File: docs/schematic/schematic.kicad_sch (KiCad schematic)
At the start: 24 parts, among them J101 Analog Levers, J12 Button Matrix, J13 Front LED, J5 Motor-PCB, J6 X-Axis, J7 Y-Axis, J8 Z-Axis, Q1 BC548, U1 ProMicroC, U101 74HC4066BQ

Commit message: update wiring
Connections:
- net GND: now also U1.11 (D8/A8); no longer U1.13 (D10/A10)
- net Matrix_Row3: now also U1.1 (TX); no longer U1.11 (D8/A8)
- no-connect marks 14 -> 13
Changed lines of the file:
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@@
-	)
-	(no_connect
-		(at 109.22 53.34)
 	)
 	(no_connect
@@
 	(wire
 		(pts
-			(xy 135.89 53.34) (xy 133.35 53.34)
-		)
-		(stroke
-			(width 0)
-			(type default)
-		)
-	)
-	(wire
-		(pts
 			(xy 170.18 29.21) (xy 167.64 29.21)
 		)
@@
 	(wire
 		(pts
-			(xy 133.35 48.26) (xy 139.7 48.26)
-		)
-		(stroke
-			(width 0)
-			(type default)
-		)
-	)
-	(wire
-		(pts
 			(xy 55.88 49.53) (xy 55.88 55.88)
 		)
@@
 	(wire
 		(pts
-			(xy 133.35 45.72) (xy 139.7 45.72)
+			(xy 133.35 45.72) (xy 137.16 45.72)
 		)
 		(stroke
@@
 	(wire
 		(pts
-			(xy 133.35 71.12) (xy 135.89 71.12)
-		)
-		(stroke
-			(width 0)
-			(type default)
-		)
-	)
-	(wire
-		(pts
-			(xy 133.35 60.96) (xy 138.43 60.96)
+			(xy 133.35 71.12) (xy 137.16 71.12)
+		)
+		(stroke
+			(width 0)
+			(type default)
+		)
+	)
+	(wire
+		(pts
+			(xy 133.35 60.96) (xy 137.16 60.96)
 		)
 		(stroke
@@
 	(wire
 		(pts
+			(xy 133.35 48.26) (xy 137.16 48.26)
+		)
+		(stroke
+			(width 0)
+			(type default)
+		)
+	)
+	(wire
+		(pts
 			(xy 166.37 93.98) (xy 198.12 93.98)
 		)
@@
 	(wire
 		(pts
-			(xy 133.35 58.42) (xy 138.43 58.42)
+			(xy 133.35 58.42) (xy 137.16 58.42)
 		)
 		(stroke
@@
 		(pts
 			(xy 245.11 138.43) (xy 245.11 139.7)
+		)
+		(stroke
+			(width 0)
+			(type default)
+		)
+	)
+	(wire
+		(pts
+			(xy 105.41 53.34) (xy 109.22 53.34)
 		)
 		(stroke
@@
 	(global_label "Matrix_Col3"
 		(shape input)
-		(at 138.43 60.96 0)
+		(at 137.16 60.96 0)
 		(fields_autoplaced yes)
 		(effects
@@
 		)
 		(property "Intersheetrefs" "${INTERSHEET_REFS}"
-			(at 152.4217 60.96 0)
+			(at 151.1517 60.96 0)
 			(effects
 				(font
@@
 		)
 	)
-	(global_label "A10"
+	(global_label "A8"
 		(shape output)
 		(at 121.92 165.1 0)
@@
 		)
 		(property "Intersheetrefs" "${INTERSHEET_REFS}"
-			(at 128.4128 165.1 0)
+			(at 127.2033 165.1 0)
 			(effects
 				(font
@@
 	(global_label "Matrix_Row2"
 		(shape output)
-		(at 139.7 45.72 0)
+		(at 137.16 45.72 0)
 		(fields_autoplaced yes)
 		(effects
@@
 		)
 		(property "Intersheetrefs" "${INTERSHEET_REFS}"
-			(at 154.357 45.72 0)
+			(at 151.817 45.72 0)
 			(effects
 				(font
@@
 		)
 	)
-	(global_label "A10"
+	(global_label "A8"
 		(shape output)
 		(at 80.01 165.1 0)
@@
 		)
 		(property "Intersheetrefs" "${INTERSHEET_REFS}"
-			(at 86.5028 165.1 0)
+			(at 85.2933 165.1 0)
 			(effects
 				(font
@@
 	(global_label "Matrix_Col2"
 		(shape input)
-		(at 138.43 58.42 0)
+		(at 137.16 58.42 0)
 		(fields_autoplaced yes)
 		(effects
@@
 		)
 		(property "Intersheetrefs" "${INTERSHEET_REFS}"
-			(at 152.4217 58.42 0)
+			(at 151.1517 58.42 0)
 			(effects
 				(font
@@
 	(global_label "A3"
 		(shape input)
-		(at 135.89 71.12 0)
+		(at 137.16 71.12 0)
 		(fields_autoplaced yes)
 		(effects
@@
 		)
 		(property "Intersheetrefs" "${INTERSHEET_REFS}"
-			(at 141.1733 71.12 0)
+			(at 142.4433 71.12 0)
 			(effects
 				(font
@@
 		)
 	)
-	(global_label "A10"
+	(global_label "A8"
 		(shape input)
-		(at 135.89 53.34 0)
+		(at 137.16 48.26 0)
 		(fields_autoplaced yes)
 		(effects
@@
 		)
 		(property "Intersheetrefs" "${INTERSHEET_REFS}"
-			(at 142.3828 53.34 0)
+			(at 142.4433 48.26 0)
 			(effects
 				(font
@@
 	(global_label "Matrix_Row3"
 		(shape output)
-		(at 139.7 48.26 0)
-		(fields_autoplaced yes)
-		(effects
-			(font
-				(size 1.27 1.27)
-			)
-			(justify left)
-		)
-		(property "Intersheetrefs" "${INTERSHEET_REFS}"
-			(at 154.357 48.26 0)
-			(effects
-				(font
-					(size 1.27 1.27)
-				)
-				(justify left)
-				(hide yes)
-			)
+		(at 105.41 53.34 180)
+		(fields_autoplaced yes)
+		(effects
+			(font
+				(size 1.27 1.27)
+			)
+			(justify right)
+		)
+		(property "Intersheetrefs" "${INTERSHEET_REFS}"
+			(at 90.753 53.34 0)
+			(effects
+				(font
+					(size 1.27 1.27)
+				)
+				(justify right)
+				(hide yes)
+			)

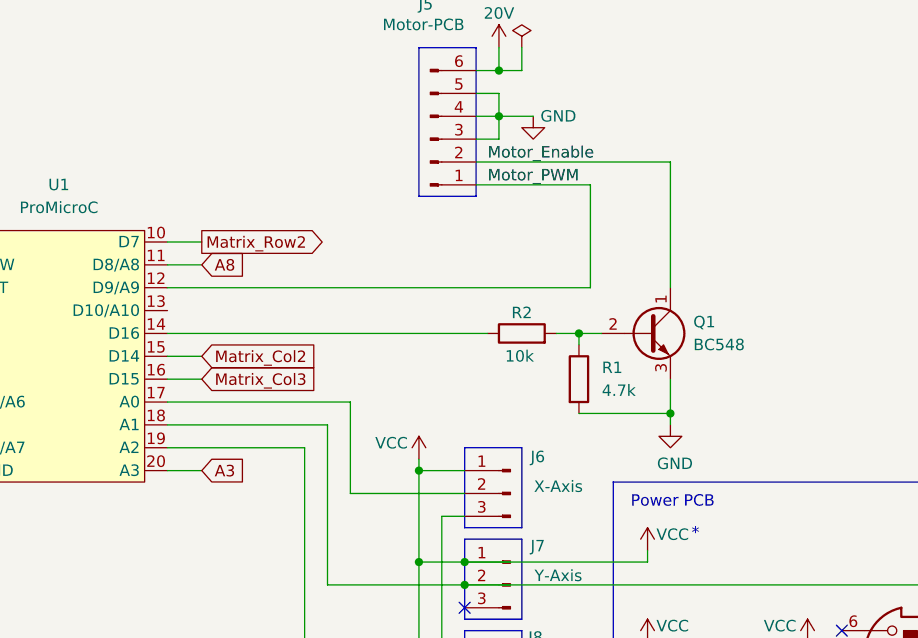
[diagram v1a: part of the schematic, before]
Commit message: update schematic
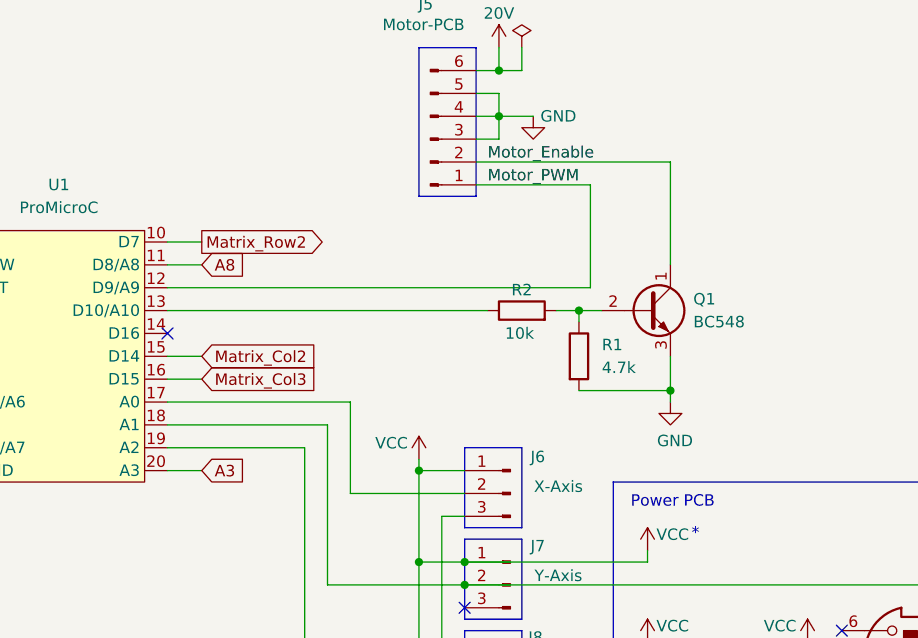
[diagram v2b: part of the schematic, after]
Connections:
- net at R2.1: now also U1.13 (D10/A10); no longer U1.14 (D16)
- no-connect marks 13 -> 14
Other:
- moved on the sheet: Q1, R1, R2
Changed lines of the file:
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@@
 	)
 	(junction
-		(at 189.23 64.77)
+		(at 189.23 62.23)
 		(diameter 0)
 		(color 0 0 0 0)
@@
 	)
 	(junction
-		(at 179.07 55.88)
-		(diameter 0)
-		(color 0 0 0 0)
-	)
-	(junction
 		(at 166.37 91.44)
 		(diameter 0)
@@
 	)
 	(junction
+		(at 179.07 53.34)
+		(diameter 0)
+		(color 0 0 0 0)
+	)
+	(junction
 		(at 170.18 31.75)
 		(diameter 0)
@@
 	)
 	(no_connect
+		(at 133.35 55.88)
+	)
+	(no_connect
 		(at 109.22 48.26)
 	)
@@
 	(wire
 		(pts
-			(xy 189.23 60.96) (xy 189.23 64.77)
-		)
-		(stroke
-			(width 0)
-			(type default)
-		)
-	)
-	(wire
-		(pts
 			(xy 59.69 63.5) (xy 69.85 63.5)
 		)
@@
 	(wire
 		(pts
-			(xy 189.23 36.83) (xy 189.23 50.8)
+			(xy 189.23 36.83) (xy 189.23 48.26)
 		)
 		(stroke
@@
 	(wire
 		(pts
-			(xy 133.35 55.88) (xy 168.91 55.88)
-		)
-		(stroke
-			(width 0)
-			(type default)
-		)
-	)
-	(wire
-		(pts
 			(xy 43.18 39.37) (xy 44.45 39.37)
 		)
@@
 	(wire
 		(pts
-			(xy 176.53 55.88) (xy 179.07 55.88)
+			(xy 176.53 53.34) (xy 179.07 53.34)
 		)
 		(stroke
@@
 	(wire
 		(pts
+			(xy 179.07 53.34) (xy 179.07 54.61)
+		)
+		(stroke
+			(width 0)
+			(type default)
+		)
+	)
+	(wire
+		(pts
 			(xy 170.18 31.75) (xy 170.18 29.21)
 		)
@@
 	(wire
 		(pts
-			(xy 179.07 55.88) (xy 181.61 55.88)
+			(xy 179.07 53.34) (xy 181.61 53.34)
 		)
 		(stroke
@@
 	(wire
 		(pts
+			(xy 189.23 58.42) (xy 189.23 62.23)
+		)
+		(stroke
+			(width 0)
+			(type default)
+		)
+	)
+	(wire
+		(pts
 			(xy 71.12 107.95) (xy 73.66 107.95)
 		)
@@
 	(wire
 		(pts
-			(xy 179.07 64.77) (xy 189.23 64.77)
+			(xy 179.07 62.23) (xy 189.23 62.23)
 		)
 		(stroke
@@
 	(wire
 		(pts
-			(xy 179.07 55.88) (xy 179.07 57.15)
-		)
-		(stroke
-			(width 0)
-			(type default)
-		)
-	)
-	(wire
-		(pts
 			(xy 133.35 48.26) (xy 137.16 48.26)
 		)
@@
 	(wire
 		(pts
-			(xy 189.23 66.04) (xy 189.23 64.77)
+			(xy 189.23 63.5) (xy 189.23 62.23)
 		)
 		(stroke
@@
 		)
 	)
+	(wire
+		(pts
+			(xy 133.35 53.34) (xy 168.91 53.34)
+		)
+		(stroke
+			(width 0)
+			(type default)
+		)
+	)
 	(label "Motor_Enable"
 		(at 168.91 36.83 0)
@@
 	(symbol
 		(lib_id "Device:R")
-		(at 172.72 55.88 90)
+		(at 172.72 53.34 90)
 		(unit 1)
 		(exclude_from_sim no)
@@
 		(dnp no)
 		(property "Reference" "R2"
-			(at 172.72 53.594 90)
+			(at 172.72 51.054 90)
 			(effects
 				(font
@@
 		)
 		(property "Value" "10k"
-			(at 172.466 58.42 90)
+			(at 172.466 55.88 90)
 			(effects
 				(font
@@
 		)
 		(property "Footprint" "Resistor_THT:R_Axial_DIN0207_L6.3mm_D2.5mm_P7.62mm_Horizontal"
-			(at 172.72 57.658 90)
+			(at 172.72 55.118 90)
 			(effects
 				(font
@@
 		)
 		(property "Datasheet" "~"
-			(at 172.72 55.88 0)
+			(at 172.72 53.34 0)
 			(effects
 				(font
@@
 		)
 		(property "Description" "Resistor"
-			(at 172.72 55.88 0)
+			(at 172.72 53.34 0)
 			(effects
 				(font
@@
 	(symbol
 		(lib_id "PCM_SparkFun-PowerSymbol:GND")
-		(at 189.23 66.04 0)
+		(at 189.23 63.5 0)
 		(unit 1)
 		(exclude_from_sim no)
@@
 		(dnp no)
 		(property "Reference" "#PWR013"
-			(at 189.23 72.39 0)
+			(at 189.23 69.85 0)
 			(effects
 				(font
@@
 		)
 		(property "Value" "GND"
-			(at 189.738 70.358 0)
+			(at 189.738 67.818 0)
 			(do_not_autoplace yes)
 			(effects
@@
 		)
 		(property "Footprint" ""
-			(at 189.23 66.04 0)
+			(at 189.23 63.5 0)
 			(effects
 				(font
@@
 		)
 		(property "Datasheet" ""
-			(at 189.23 66.04 0)
+			(at 189.23 63.5 0)
 			(effects
 				(font
@@
 		)
 		(property "Description" "Power symbol creates a global label with name \"GND\" , ground"
-			(at 189.23 74.93 0)
+			(at 189.23 72.39 0)
 			(effects
 				(font
@@
 	(symbol
 		(lib_id "Device:R")
-		(at 179.07 60.96 0)
+		(at 179.07 58.42 0)
 		(unit 1)
 		(exclude_from_sim no)
@@
 		(fields_autoplaced yes)
 		(property "Reference" "R1"
-			(at 181.61 59.6899 0)
+			(at 181.61 57.1499 0)
 			(effects
 				(font
@@
 		)
 		(property "Value" "4.7k"
-			(at 181.61 62.2299 0)
+			(at 181.61 59.6899 0)
 			(effects
 				(font
@@
 		)
 		(property "Footprint" "Resistor_THT:R_Axial_DIN0207_L6.3mm_D2.5mm_P7.62mm_Horizontal"
-			(at 177.292 60.96 90)
+			(at 177.292 58.42 90)
 			(effects
 				(font
@@
 		)
 		(property "Datasheet" "~"
-			(at 179.07 60.96 0)
+			(at 179.07 58.42 0)
 			(effects
 				(font
@@
 		)
 		(property "Description" "Resistor"
-			(at 179.07 60.96 0)
+			(at 179.07 58.42 0)
 			(effects
 				(font
@@
 	(symbol
 		(lib_id "Transistor_BJT:BC548")
-		(at 186.69 55.88 0)
+		(at 186.69 53.34 0)
 		(unit 1)
 		(exclude_from_sim no)
@@
 		(fields_autoplaced yes)
 		(property "Reference" "Q1"
-			(at 191.77 54.6099 0)
+			(at 191.77 52.0699 0)
 			(effects
 				(font
@@
 		)
 		(property "Value" "BC548"
-			(at 191.77 57.1499 0)
+			(at 191.77 54.6099 0)
 			(effects
 				(font
@@
 		)
 		(property "Footprint" "Package_TO_SOT_THT:TO-92_Inline"
-			(at 191.77 57.785 0)
+			(at 191.77 55.245 0)
 			(effects
 				(font
@@
 		)
 		(property "Datasheet" "https://www.onsemi.com/pub/Collateral/BC550-D.pdf"
-			(at 186.69 55.88 0)
+			(at 186.69 53.34 0)
 			(effects
 				(font
@@
 		)
 		(property "Description" "0.1A Ic, 30V Vce, Small Signal NPN Transistor, TO-92"
-			(at 186.69 55.88 0)
+			(at 186.69 53.34 0)
 			(effects
 				(font
@@
 		)
 		(property "Sim.Device" "NPN"
-			(at 186.69 55.88 0)
+			(at 186.69 53.34 0)
 			(effects
 				(font
@@
 		)
 		(property "Sim.Pins" "1=C 2=B 3=E"
-			(at 186.69 55.88 0)
+			(at 186.69 53.34 0)
 			(effects
 				(font
